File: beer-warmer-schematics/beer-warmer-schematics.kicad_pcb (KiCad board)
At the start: 4 copper layers, 60 x 50 mm, 27 parts, among them J1 USB_C_Receptacle_USB2.0_14P, J2 Screw_Terminal_01x02, J3 Conn_01x07_Socket, J4 Conn_01x07_Socket, J5 Conn_01x04_Pin, J6 Screw_Terminal_01x03, Q1 AOD4184A, U2 LM2596S-5, U3 CH224K

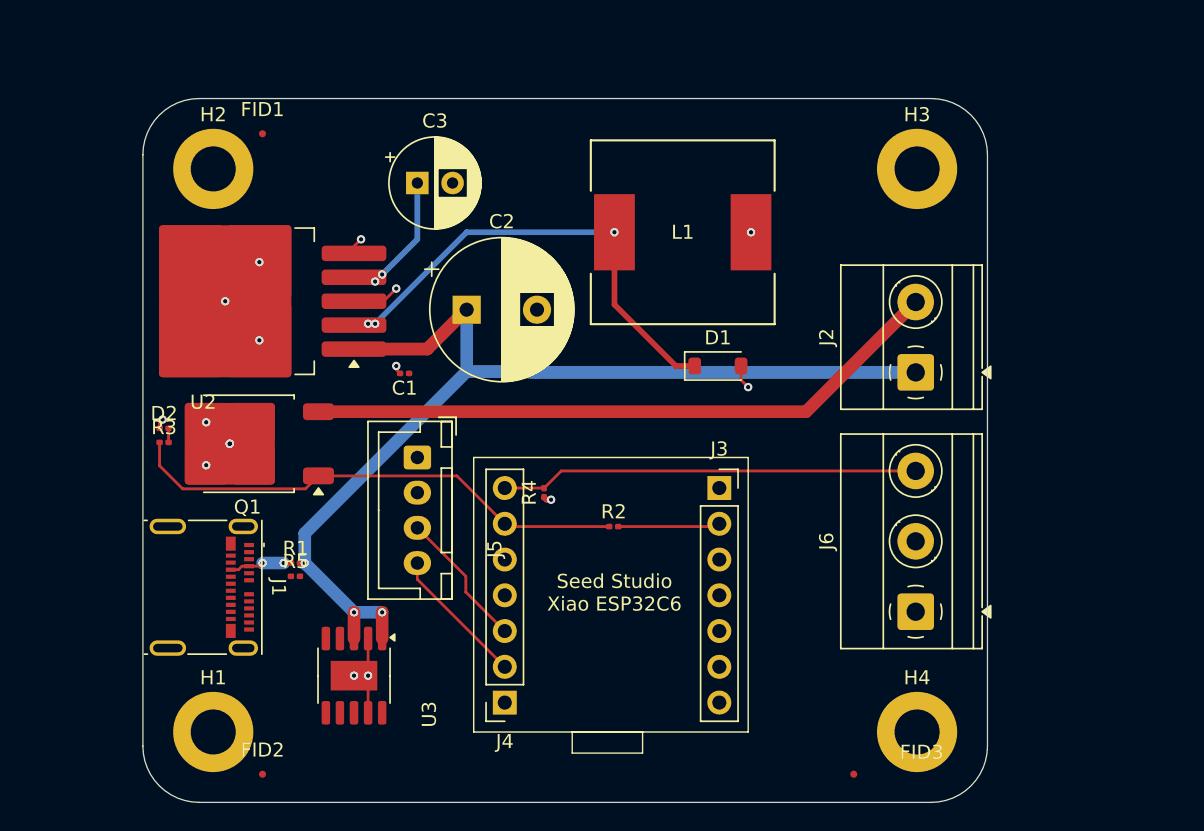
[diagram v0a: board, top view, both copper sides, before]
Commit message: cleanup add more lcsc numbers
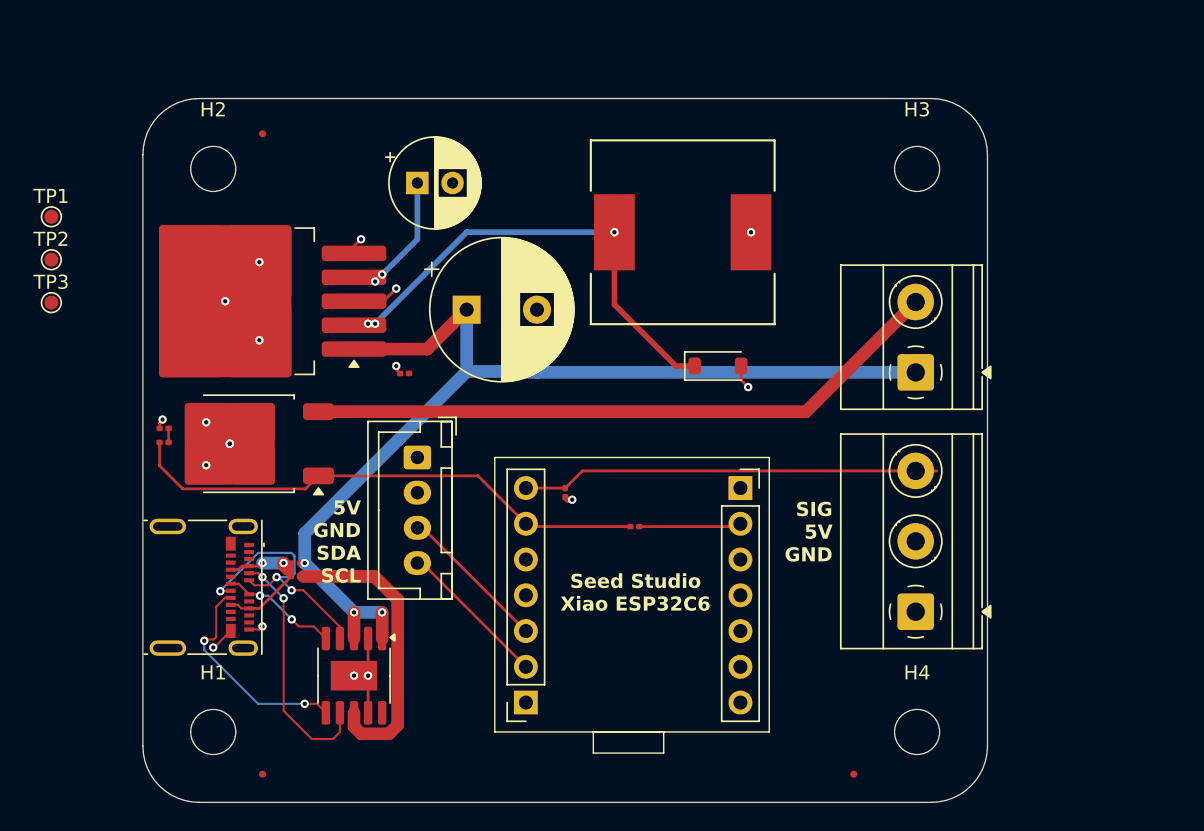
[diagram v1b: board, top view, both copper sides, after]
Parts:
- added TP1: TestPoint, TestPoint:TestPoint_Pad_D1.0mm, F.Cu at (103.5, 79.4)
- added TP2: TestPoint, TestPoint:TestPoint_Pad_D1.0mm, F.Cu at (103.5, 82.5)
- added TP3: TestPoint, TestPoint:TestPoint_Pad_D1.0mm, F.Cu at (103.5, 85.5)
- H1, H2, H3, H4: footprint MountingHole:MountingHole_3.2mm_M3_ISO7380_Pad -> MountingHole:MountingHole_3.2mm_M3
- moved J3 1.50 mm to (152.4, 98.7)
- moved J4 1.50 mm to (137.2, 113.9)
- moved R2 1.50 mm to (144.9, 101.4)
- moved R4 1.50 mm to (140.0, 99.0)
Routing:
- net Net-(U3-VBUS): track 0.00 -> 20.9 mm
- net Net-(U3-DP): track 0.00 -> 19.0 mm, vias 0 -> 3
- net Net-(J1-CC1): track 0.00 -> 17.6 mm, vias 0 -> 2
- net Net-(J1-CC2): track 0.00 -> 15.5 mm, vias 0 -> 2
- net Net-(U3-DM): track 0.00 -> 8.37 mm, vias 0 -> 2
- net Net-(J1-VBUS-PadA4): track 4.48 -> 10.4 mm
- net GND: track 21.0 -> 23.8 mm, vias 14 -> 16
- net D1: track 36.2 -> 37.7 mm
- net SDA: track 9.90 -> 10.7 mm
- net SCL: track 9.94 -> 10.8 mm
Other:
- board text added: "5V GND SDA SCL"
- board text added: "SIG 5V GND"

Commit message: redid board layout
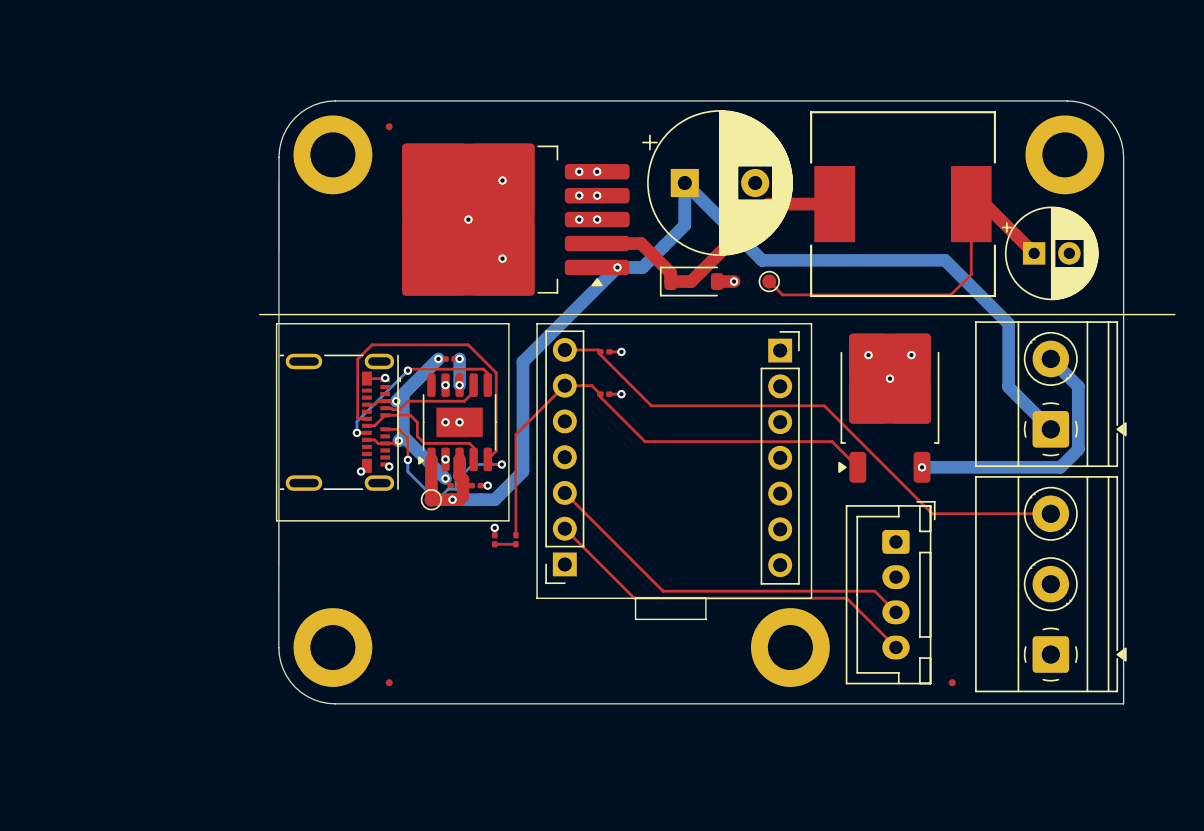
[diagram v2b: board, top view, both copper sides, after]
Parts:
- removed TP3: TestPoint, TestPoint:TestPoint_Pad_D1.0mm
- H1, H2, H3, H4: footprint MountingHole:MountingHole_3.2mm_M3 -> MountingHole:MountingHole_3.2mm_M3_DIN965_Pad
- moved TP2 51.0 mm to (154.5, 84.0)
- moved Q1 45.8 mm to (163.1, 92.2), turned to 90 degrees
- moved C3 44.1 mm to (173.3, 82.0)
- moved H1 41.9 mm to (123.5, 75.0)
- moved H2 35.0 mm to (123.5, 110.0)
- moved J5 34.5 mm to (163.5, 102.5)
- moved TP1 33.7 mm to (130.5, 99.5)
- moved R3 25.9 mm to (136.5, 102.3), turned to -90 degrees
- moved D2 24.8 mm to (135.0, 102.3), turned to -90 degrees
- moved U3 19.5 mm to (132.5, 94.0), turned to 90 degrees
- moved R5 18.9 mm to (131.8, 89.5)
- moved U2 18.2 mm to (134.6, 79.6)
- moved C2 17.9 mm to (148.5, 77.0)
- moved L1 15.8 mm to (164.0, 78.5)
- moved J1 15.2 mm to (124.0, 94.0)
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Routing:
- net Net-(U3-DM): track 8.37 -> 36.4 mm
- net Net-(J2-Pin_2): track 45.7 -> 18.9 mm, vias 0 -> 1
- net Net-(U3-VBUS): track 20.9 -> 2.22 mm, vias 0 -> 2
- net GND: track 23.8 -> 5.33 mm, vias 16 -> 21
- net +5V: track 8.82 -> 27.1 mm, vias 4 -> 3
- net SDA: track 10.7 -> 27.0 mm
- net SCL: track 10.8 -> 27.0 mm
- net Net-(D1-K): track 32.8 -> 20.6 mm, vias 3 -> 0
- net Net-(J1-CC1): track 17.6 -> 7.33 mm, vias 2 -> 0
- net D0: track 29.7 -> 39.5 mm
- net Net-(U3-DP): track 19.0 -> 10.3 mm, vias 3 -> 0
- net Net-(J1-VBUS-PadA4): track 10.4 -> 17.7 mm, vias 2 -> 4
- net D1: track 37.7 -> 35.4 mm
- net Net-(J1-CC2): track 15.5 -> 13.3 mm
- net VDD: track 75.4 -> 76.3 mm, vias 3 -> 2
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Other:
- board size 60 x 50 mm -> 60 x 42.8 mm
- board text removed: "5V GND SDA SCL"
- board text removed: "SIG 5V GND"
- board text removed: "Seed Studio Xiao ESP32C6"

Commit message: styling
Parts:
- moved D2 4.31 mm to (135.0, 106.7)
- moved R3 4.31 mm to (136.5, 106.7)
- moved J5 0.71 mm to (163.0, 103.0)
- moved H4 0.50 mm to (155.5, 110.0)
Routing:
- net D1: track 35.4 -> 39.7 mm
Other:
- board text added: "12V USB PD"
- board text added: "Beer Thermostat"
- board text added: "Heat enabled"
- board text added: "Heater out"
- board text added: "OLED"
- board text added: "REV 1.0"
- board text added: "SIG 5V GND"
- board text added: "Seeed Studio Xiao ESP32C6"
- board text added: "Step-down"
- board text added: "Switch"
- board text added: "TP 12V"
- board text added: "TP 5V"
- board text added: "Temp probe"
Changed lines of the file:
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@@
 	(footprint "Connector_JST:JST_XH_B4B-XH-A_1x04_P2.50mm_Vertical"
 		(layer "F.Cu")
-		(at 163.5 102.5 -90)
+		(at 163 103 -90)
 		(descr "JST XH series connector, B4B-XH-A (http://www.jst-mfg.com/product/pdf/eng/eXH.pdf), generated with kicad-footprint-generator")
 		(tags "connector JST XH vertical")
@@
 	(footprint "Resistor_SMD:R_0201_0603Metric"
 		(layer "F.Cu")
-		(at 135 102.345 -90)
+		(at 135 106.655 -90)
 		(descr "Resistor SMD 0201 (0603 Metric), square (rectangular) end terminal, IPC_7351 nominal, (Body size source: https://www.vishay.com/docs/20052/crcw0201e3.pdf), generated with kicad-footprint-generator")
 		(tags "resistor")
@@
 	(footprint "MountingHole:MountingHole_3.2mm_M3_DIN965_Pad"
 		(layer "F.Cu")
-		(at 156 110)
+		(at 155.5 110)
 		(descr "Mounting Hole 3.2mm, M3, DIN965")
 		(tags "mounting hole 3.2mm m3 din965")
@@
 	(footprint "Resistor_SMD:R_0201_0603Metric"
 		(layer "F.Cu")
-		(at 136.5 102.345 -90)
+		(at 136.5 106.655 -90)
 		(descr "Resistor SMD 0201 (0603 Metric), square (rectangular) end terminal, IPC_7351 nominal, (Body size source: https://www.vishay.com/docs/20052/crcw0201e3.pdf), generated with kicad-footprint-generator")
 		(tags "resistor")
@@
 	(gr_rect
 		(start 119.5 87)
-		(end 136 101)
+		(end 136 104)
+		(stroke
+			(width 0.1)
+			(type default)
+		)
+		(fill no)
+		(layer "F.SilkS")
+	)
+	(gr_rect
+		(start 159 87)
+		(end 168.5 99)
 		(stroke
 			(width 0.1)
@@
 		(layer "F.SilkS")
 	)
+	(gr_rect
+		(start 159 99.5)
+		(end 168.5 113.5)
+		(stroke
+			(width 0.1)
+			(type default)
+		)
+		(fill no)
+		(layer "F.SilkS")
+	)
+	(gr_rect
+		(start 134.318708 105.704328)
+		(end 137.138811 107.648185)
+		(stroke
+			(width 0.1)
+			(type default)
+		)
+		(fill no)
+		(layer "F.SilkS")
+	)
 	(gr_arc
 		(start 123.66 114)
@@
 		(layer "Edge.Cuts")
 	)
+	(gr_text "Beer Thermostat"
+		(at 127 111 0)
+		(layer "F.SilkS" knockout)
+		(effects
+			(font
+				(size 2 2)
+				(thickness 0.2)
+				(bold yes)
+			)
+			(justify left bottom)
+		)
+	)
+	(gr_text "OLED"
+		(at 168 109.5 90)
+		(layer "F.SilkS")
+		(effects
+			(font
+				(size 1 1)
+				(thickness 0.2)
+				(bold yes)
+			)
+			(justify left bottom)
+		)
+	)
+	(gr_text "Seeed Studio\nXiao ESP32C6"
+		(at 150 96.5 90)
+		(layer "F.SilkS")
+		(effects
+			(font
+				(size 1.5 1.5)
+				(thickness 0.3)
+				(bold yes)
+			)
+			(justify bottom)
+		)
+	)
+	(gr_text "Step-down"
+		(at 131.5 73.5 0)
+		(layer "F.SilkS")
+		(effects
+			(font
+				(size 1.5 1.5)
+				(thickness 0.3)
+				(bold yes)
+			)
+			(justify left bottom)
+		)
+	)
+	(gr_text "12V USB PD"
+		(at 120.5 103 0)
+		(layer "F.SilkS")
+		(effects
+			(font
+				(size 1.5 1.5)
+				(thickness 0.3)
+				(bold yes)
+			)
+			(justify left bottom)
+		)
+	)
+	(gr_text "Heat enabled"
+		(at 127.5 105.5 0)
+		(layer "F.SilkS")
+		(effects
+			(font
+				(size 1 1)
+				(thickness 0.1)
+			)
+			(justify left bottom)
+		)
+	)
+	(gr_text "TP 5V"
+		(at 152.5 86 0)
+		(layer "F.SilkS")
+		(effects
+			(font
+				(size 0.8 0.8)
+				(thickness 0.1)
+			)
+			(justify left bottom)
+		)
+	)
+	(gr_text "Switch"
+		(at 168 95.5 90)
+		(layer "F.SilkS")
+		(effects
+			(font
+				(size 1 1)
+				(thickness 0.2)
+				(bold yes)
+			)
+			(justify left bottom)
+		)
+	)
+	(gr_text "TP 12V"
+		(at 125 100.5 0)
+		(layer "F.SilkS")
+		(effects
+			(font
+				(size 0.8 0.8)
+				(thickness 0.1)
+			)
+			(justify left bottom)
+		)
+	)
+	(gr_text "REV 1.0"
+		(at 130.5 113.5 0)
+		(layer "F.SilkS" knockout)
+		(effects
+			(font
+				(size 1.5 1.5)
+				(thickness 0.2)
+				(bold yes)
+			)
+			(justify left bottom)
+		)
+	)
+	(gr_text "Heater\nout"
+		(at 171.5 93.5 0)
+		(layer "B.SilkS")
+		(effects
+			(font
+				(size 1 1)
+				(thickness 0.2)
+				(bold yes)
+			)
+			(justify left bottom mirror)
+		)
+	)
+	(gr_text "SIG\n5V\nGND"
+		(at 171.5 108.5 0)
+		(layer "B.SilkS")
+		(effects
+			(font
+				(size 1.5 1.5)
+				(thickness 0.3)
+				(bold yes)
+			)
+			(justify left bottom mirror)
+		)
+	)
+	(gr_text "Temp\nprobe"
+		(at 171.5 101 0)
+		(layer "B.SilkS")
+		(effects
+			(font
+				(size 1 1)
+				(thickness 0.2)
+				(bold yes)
+			)
+			(justify left bottom mirror)
+		)
+	)
 	(segment
 		(start 132.741 98.086154)
@@
 	)
 	(segment
-		(start 135 102.025)
-		(end 135 101.5)
+		(start 135 106.335)
+		(end 135 105.81)
 		(width 0.2)
 		(layer "F.Cu")
@@
 	)
 	(via
-		(at 135 101.5)
+		(at 135 105.81)
 		(size 0.6)
 		(drill 0.3)
@@
 	)
 	(segment
-		(start 136.5 102.665)
-		(end 135 102.665)
+		(start 136.5 106.975)
+		(end 135 106.975)
 		(width 0.2)
 		(layer "F.Cu")
@@
 	)
 	(segment
-		(start 144.915 106.5)
-		(end 160 106.5)
+		(start 162.5 110.5)
+		(end 158.5 106.5)
+		(width 0.2)
+		(layer "F.Cu")
+		(net 17)
+	)
+	(segment
+		(start 163 110.5)
+		(end 162.5 110.5)
 		(width 0.2)
 		(layer "F.Cu")
@@
 	)
 	(segment
-		(start 160 106.5)
-		(end 163.5 110)
+		(start 144.915 106.5)
+		(end 158.5 106.5)
 		(width 0.2)
 		(layer "F.Cu")
@@
 	)
 	(segment
-		(start 146.955 106)
-		(end 162 106)
+		(start 161 106)
+		(end 163 108)
 		(width 0.2)
 		(layer "F.Cu")
@@
 	)
 	(segment
-		(start 162 106)
-		(end 163.5 107.5)
+		(start 146.955 106)
+		(end 160 106)
 		(width 0.2)
 		(layer "F.Cu")
@@
 	)
 	(segment
+		(start 160 106)
+		(end 161 106)
+		(width 0.2)
+		(layer "F.Cu")
+		(net 21)
+	)
+	(segment
 		(start 139.975 91.4)
 		(end 141.9 91.4)
@@
 	)
 	(segment
-		(start 136.5 94.875)
-		(end 139.975 91.4)
+		(start 141.9 91.4)
+		(end 142.5 92)
 		(width 0.2)
 		(layer "F.Cu")
@@
 	)
 	(segment
-		(start 141.9 91.4)
-		(end 142.5 92)
+		(start 158.966838 95.374338)
+		(end 145.674339 95.374338)
 		(width 0.2)
 		(layer "F.Cu")
@@
 	)
 	(segment
-		(start 158.966838 95.374338)
-		(end 145.674339 95.374338)
+		(start 136.5 94.875)
+		(end 136.5 106.335)
 		(width 0.2)
 		(layer "F.Cu")
@@
 	)
 	(segment
-		(start 136.5 102.025)
+		(start 139.975 91.4)
 		(end 136.5 94.875)
 		(width 0.2)

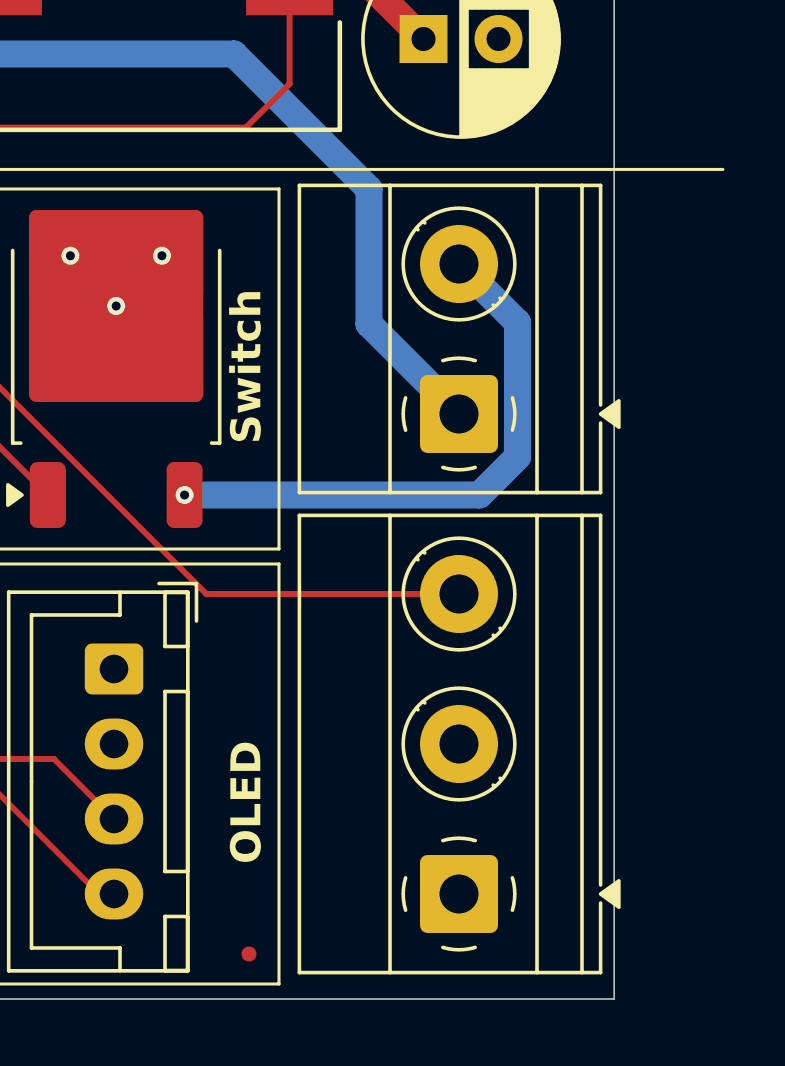
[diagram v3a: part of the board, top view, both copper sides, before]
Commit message: fix screw terminal component
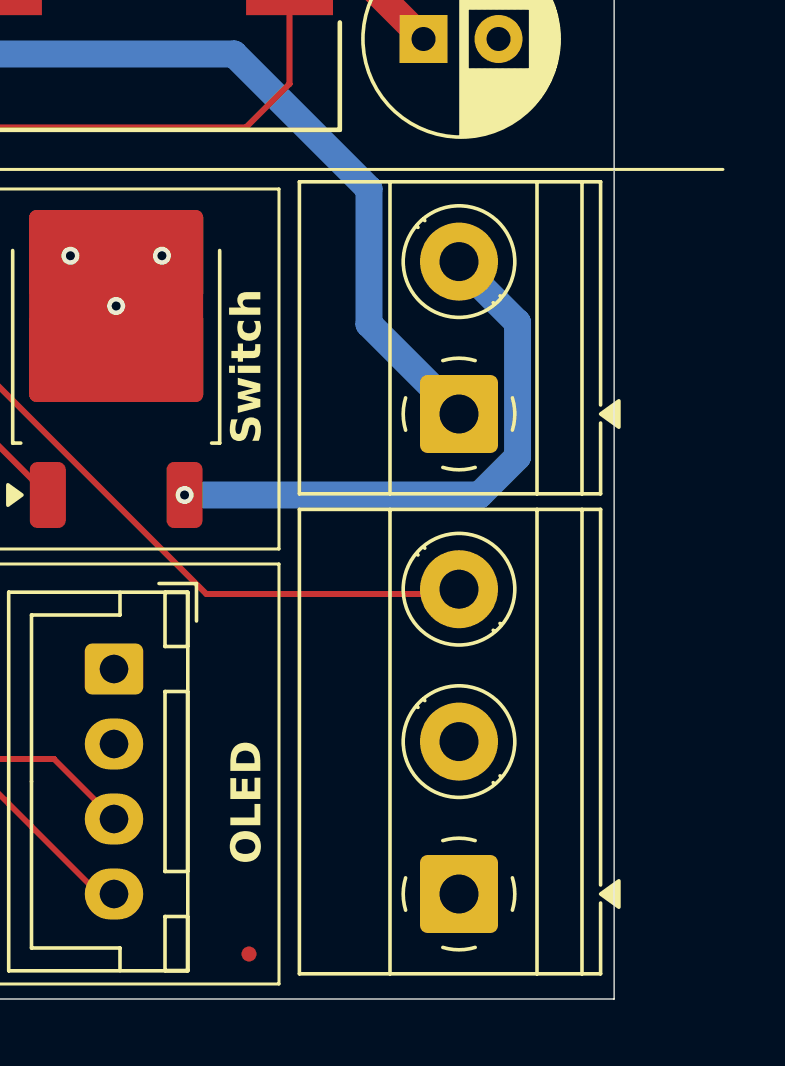
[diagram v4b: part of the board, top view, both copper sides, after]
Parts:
- J2: footprint TerminalBlock_Phoenix:TerminalBlock_Phoenix_MKDS-1,5-2_1x02_P5.00mm_Horizontal -> TerminalBlock_Phoenix:TerminalBlock_Phoenix_MKDS-1,5-2-5.08_1x02_P5.08mm_Horizontal
- J6: footprint TerminalBlock_Phoenix:TerminalBlock_Phoenix_MKDS-1,5-3_1x03_P5.00mm_Horizontal -> TerminalBlock_Phoenix:TerminalBlock_Phoenix_MKDS-1,5-3-5.08_1x03_P5.08mm_Horizontal

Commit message: cleanup
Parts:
- moved C3 50.8 mm to (122.5, 82.0)
- moved H4 20.0 mm to (175.5, 110.0)
- moved J2 7.45 mm to (174.5, 87.0)
- moved J6 6.92 mm to (174.5, 103.6)
- moved FID3 4.00 mm to (171.5, 112.5)
- moved L1 2.23 mm to (161.8, 78.9)
- moved C2 1.50 mm to (147.0, 77.0)
- moved D2 1.23 mm to (135.3, 105.5)
- moved R3 1.23 mm to (136.8, 105.5)
- moved U2 0.72 mm to (133.9, 79.8)
- moved R2 0.62 mm to (142.7, 91.4)
- moved TP2 0.50 mm to (154.0, 84.0)
- moved J5 0.14 mm to (163.0, 102.9)
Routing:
- net VDD: track 76.3 -> 1.59 mm, vias 2 -> 8
- net Net-(U3-DM): track 36.4 -> 13.1 mm, vias 2 -> 3
- net +5V: track 27.1 -> 12.9 mm, vias 3 -> 5
- net GND: track 5.33 -> 15.3 mm, vias 21 -> 0
- net Net-(J1-VBUS-PadA4): track 17.7 -> 21.2 mm, vias 4 -> 8
- net Net-(J1-CC2): track 13.3 -> 15.4 mm
- net Net-(D1-K): track 20.6 -> 22.5 mm, vias 0 -> 4
- net D1: track 39.7 -> 41.2 mm, vias 0 -> 2
- net D0: track 39.5 -> 40.6 mm, vias 0 -> 1
- net Net-(U3-DP): track 10.3 -> 9.74 mm, vias 0 -> 2
- net Net-(J2-Pin_2): track 18.9 -> 18.5 mm, vias 1 -> 2
- net Net-(J1-CC1): track 7.33 -> 6.96 mm, vias 0 -> 2
- net Net-(U3-VBUS): track 2.22 -> 1.91 mm, vias 2 -> 0
- added copper zone on In1.Cu, net +5V
- added copper zone on F.Cu, net GND
- added copper zone on In2.Cu, net VDD
- removed copper zone on In2.Cu, net +5V
- removed copper zone on In1.Cu, net GND
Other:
- outline, holes or cut-outs redrawn
- board text added: "- +"
